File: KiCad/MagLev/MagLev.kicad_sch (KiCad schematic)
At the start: 71 parts, among them J1 FC681465S, Q11 MMBT3904, Q12 AOD442G, Q13 AOD442G, Q18 ZX5T1951GTA, Q5 ZX5T1951GTA, U10 DRV5505, U11 DRV5505, U12 DRV5505, U13 MCP1402, U14 MCP1402, U3 L78L05_SO8, U4 TL431A, U5 LM393, X1 L_Ferrite, X2 L_Ferrite, Y1 L_Ferrite, Y2 L_Ferrite, Y5 L_Ferrite, Y6 L_Ferrite, Y8 L_Ferrite, Y9 L_Ferrite

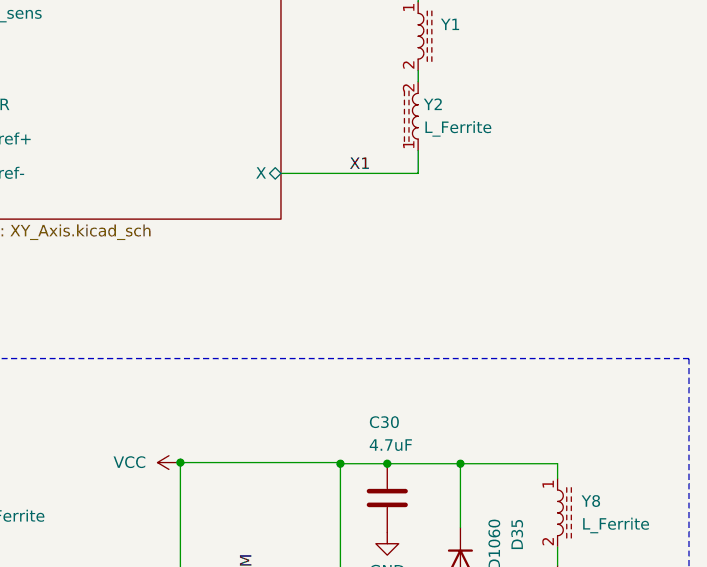
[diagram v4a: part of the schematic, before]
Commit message: Remove silkscreen components from back layer. Cleanup schematic and pcb.
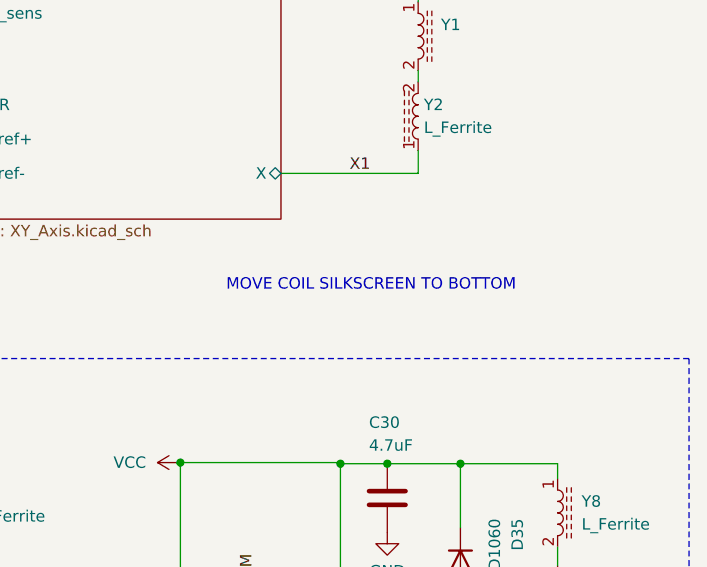
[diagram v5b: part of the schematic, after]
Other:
- note added: "MOVE COIL SILKSCREEN TO BOTTOM"
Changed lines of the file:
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@@
+    (effects (font (size 1.27 1.27)) (justify left bottom))
+  )
+  (text "MOVE COIL SILKSCREEN TO BOTTOM" (at 232.664 93.472 0)
     (effects (font (size 1.27 1.27)) (justify left bottom))
   )

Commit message: Update LED PCB reference after adding new LED schematic sheet.
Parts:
- DS1: PN (none) -> SML-LXT0805IW-TR; Part SML-LXT0805IW-TR -> (none)

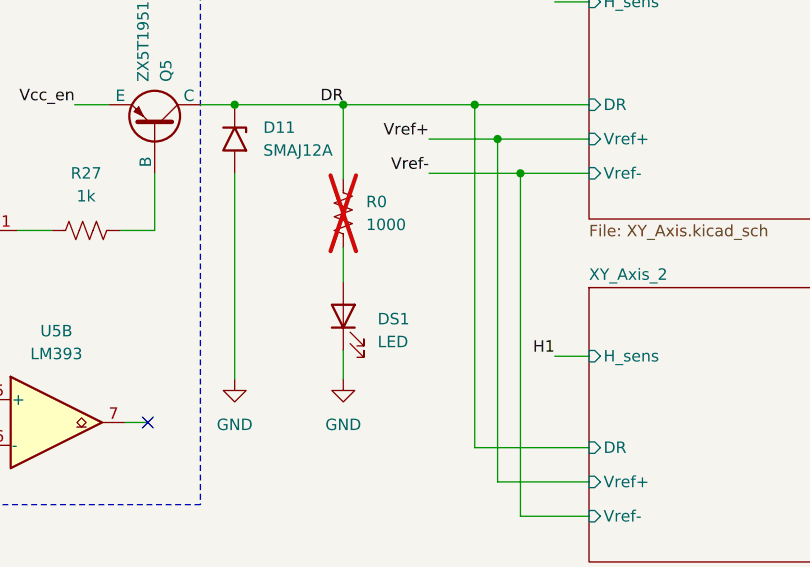
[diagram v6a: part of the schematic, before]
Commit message: Update BOM with JLCPCB PNs.
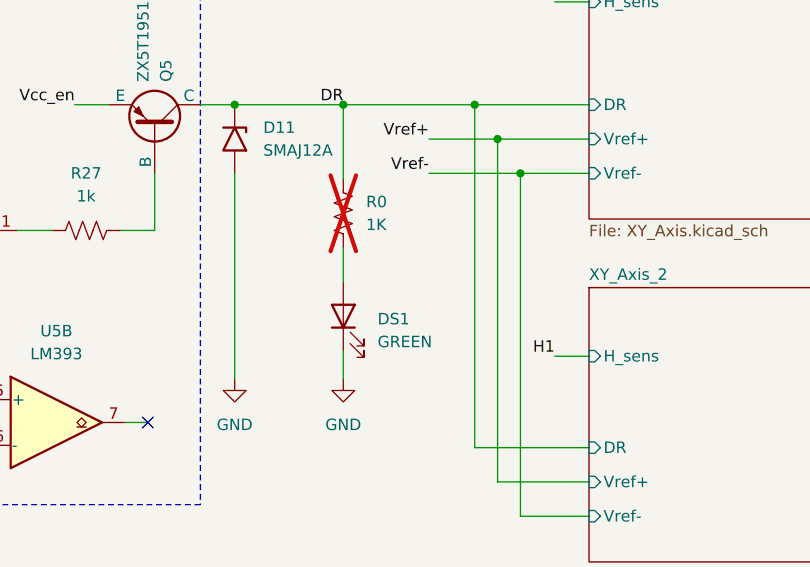
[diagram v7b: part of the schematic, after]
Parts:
- C10: JLC Part Number (none) -> C1710
- C19, C2, C20, C32, C33, C34, C35, C5: JLC Part Number (none) -> C28233
- C22, C23: JLC Part Number (none) -> C249974
- C29, C30, C31: JLC Part Number (none) -> C1779
- C9: JLC Part Number (none) -> C1740
- D34, D35: JLC Part Number (none) -> C174026
- DS1: value LED -> GREEN; JLC Part Number (none) -> C2297
- R0: value 1000 -> 1K
- R14, R16, R17, R7: JLC Part Number (none) -> C118848
- R15: JLC Part Number (none) -> C4328
- R18, R26: JLC Part Number (none) -> C25270
- R2, R27, R40, R51, R66: JLC Part Number (none) -> C17513
- R50: JLC Part Number (none) -> C17514
- R67: JLC Part Number (none) -> C17414
- U13, U14: JLC Part Number (none) -> C128573
- U3: JLC Part Number (none) -> C42738
- U4: JLC Part Number (none) -> C23892
- U5: JLC Part Number (none) -> C7955
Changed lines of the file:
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@@
       (effects (font (size 1.27 1.27)) hide)
     )
-    (property "JLC Part Number" "" (at 76.073 141.605 0)
+    (property "JLC Part Number" "C249974" (at 76.073 141.605 0)
       (effects (font (size 1.27 1.27)) hide)
     )
@@
       (effects (font (size 1.27 1.27)) hide)
     )
-    (property "JLC Part Number" "" (at 64.135 141.605 0)
+    (property "JLC Part Number" "C249974" (at 64.135 141.605 0)
       (effects (font (size 1.27 1.27)) hide)
     )
@@
       (effects (font (size 1.27 1.27)) hide)
     )
-    (property "JLC Part Number" "" (at 191.516 122.555 0)
+    (property "JLC Part Number" "C174026" (at 191.516 122.555 0)
       (effects (font (size 1.27 1.27)) hide)
     )
@@
       (effects (font (size 1.27 1.27)) hide)
     )
-    (property "JLC Part Number" "" (at 110.49 159.893 0)
+    (property "JLC Part Number" "C23892" (at 110.49 159.893 0)
       (effects (font (size 1.27 1.27)) hide)
     )
@@
       (effects (font (size 1.27 1.27)) hide)
     )
-    (property "JLC Part Number" "" (at 160.401 138.049 0)
+    (property "JLC Part Number" "C28233" (at 160.401 138.049 0)
       (effects (font (size 1.27 1.27)) hide)
     )
@@
       (effects (font (size 1.27 1.27)) hide)
     )
-    (property "JLC Part Number" "" (at 41.91 173.482 0)
+    (property "JLC Part Number" "C1740" (at 41.91 173.482 0)
       (effects (font (size 1.27 1.27)) hide)
     )
@@
       (effects (font (size 1.27 1.27)) hide)
     )
-    (property "JLC Part Number" "" (at 128.27 152.273 0)
+    (property "JLC Part Number" "C118848" (at 128.27 152.273 0)
       (effects (font (size 1.27 1.27)) hide)
     )
@@
       (effects (font (size 1.27 1.27)) hide)
     )
-    (property "JLC Part Number" "" (at 145.288 69.85 0)
+    (property "JLC Part Number" "C7955" (at 145.288 69.85 0)
       (effects (font (size 1.27 1.27)) hide)
     )
@@
       (effects (font (size 1.27 1.27)) hide)
     )
-    (property "JLC Part Number" "" (at 133.35 48.514 0)
+    (property "JLC Part Number" "C7955" (at 133.35 48.514 0)
       (effects (font (size 1.27 1.27)) hide)
     )
@@
       (effects (font (size 1.27 1.27)) hide)
     )
-    (property "JLC Part Number" "" (at 168.783 134.366 0)
+    (property "JLC Part Number" "C17513" (at 168.783 134.366 0)
       (effects (font (size 1.27 1.27)) hide)
     )
@@
       (effects (font (size 1.27 1.27)) hide)
     )
-    (property "JLC Part Number" "" (at 46.99 41.91 0)
+    (property "JLC Part Number" "C28233" (at 46.99 41.91 0)
       (effects (font (size 1.27 1.27)) hide)
     )
@@
       (effects (font (size 1.27 1.27)) hide)
     )
-    (property "JLC Part Number" "" (at 128.27 180.213 0)
+    (property "JLC Part Number" "C28233" (at 128.27 180.213 0)
       (effects (font (size 1.27 1.27)) hide)
     )
@@
       (effects (font (size 1.27 1.27)) hide)
     )
-    (property "JLC Part Number" "" (at 101.473 141.605 0)
+    (property "JLC Part Number" "C28233" (at 101.473 141.605 0)
       (effects (font (size 1.27 1.27)) hide)
     )
@@
       (effects (font (size 1.27 1.27)) hide)
     )
-    (property "JLC Part Number" "" (at 227.584 138.938 0)
+    (property "JLC Part Number" "C28233" (at 227.584 138.938 0)
       (effects (font (size 1.27 1.27)) hide)
     )
@@
       (effects (font (size 1.27 1.27)) hide)
     )
-    (property "JLC Part Number" "" (at 86.233 149.225 0)
+    (property "JLC Part Number" "C17514" (at 86.233 149.225 0)
       (effects (font (size 1.27 1.27)) hide)
     )
@@
       (effects (font (size 1.27 1.27)) hide)
     )
-    (property "JLC Part Number" "" (at 65.405 173.482 0)
+    (property "JLC Part Number" "C1710" (at 65.405 173.482 0)
       (effects (font (size 1.27 1.27)) hide)
     )
@@
       (effects (font (size 1.27 1.27)) (justify right))
     )
-    (property "Value" "LED" (at 180.975 60.8965 90)
+    (property "Value" "GREEN" (at 180.975 60.8965 90)
       (effects (font (size 1.27 1.27)) (justify right))
     )
@@
       (effects (font (size 1.27 1.27)) hide)
     )
-    (property "JLC Part Number" "" (at 177.165 58.039 0)
+    (property "JLC Part Number" "C2297" (at 177.165 58.039 0)
       (effects (font (size 1.27 1.27)) hide)
     )
@@
       (effects (font (size 1.27 1.27)) hide)
     )
-    (property "JLC Part Number" "" (at 235.966 135.255 0)
+    (property "JLC Part Number" "C17513" (at 235.966 135.255 0)
       (effects (font (size 1.27 1.27)) hide)
     )
@@
       (effects (font (size 1.27 1.27)) hide)
     )
-    (property "JLC Part Number" "" (at 56.388 80.518 0)
+    (property "JLC Part Number" "C17414" (at 56.388 80.518 0)
       (effects (font (size 1.27 1.27)) hide)
     )
@@
       (effects (font (size 1.27 1.27)) hide)
     )
-    (property "JLC Part Number" "" (at 63.5 85.09 0)
+    (property "JLC Part Number" "C17513" (at 63.5 85.09 0)
       (effects (font (size 1.27 1.27)) hide)
     )
@@
       (effects (font (size 1.27 1.27)) hide)
     )
-    (property "JLC Part Number" "" (at 116.84 45.974 0)
+    (property "JLC Part Number" "C118848" (at 116.84 45.974 0)
       (effects (font (size 1.27 1.27)) hide)
     )
@@
       (effects (font (size 1.27 1.27)) hide)
     )
-    (property "JLC Part Number" "" (at 76.2 41.656 0)
+    (property "JLC Part Number" "C28233" (at 76.2 41.656 0)
       (effects (font (size 1.27 1.27)) hide)
     )
@@
       (effects (font (size 1.27 1.27)) hide)
     )
-    (property "JLC Part Number" "" (at 183.769 115.443 0)
+    (property "JLC Part Number" "C1779" (at 183.769 115.443 0)
       (effects (font (size 1.27 1.27)) hide)
     )
@@
       (effects (font (size 1.27 1.27)) hide)
     )
-    (property "JLC Part Number" "" (at 125.73 63.754 0)
+    (property "JLC Part Number" "C118848" (at 125.73 63.754 0)
       (effects (font (size 1.27 1.27)) hide)
     )
@@
       (effects (font (size 1.27 1.27)) hide)
     )
-    (property "JLC Part Number" "" (at 29.718 87.122 0)
+    (property "JLC Part Number" "C7955" (at 29.718 87.122 0)
       (effects (font (size 1.27 1.27)) hide)
     )
@@
       (effects (font (size 1.27 1.27)) hide)
     )
-    (property "JLC Part Number" "" (at 78.613 96.52 0)
+    (property "JLC Part Number" "C17513" (at 78.613 96.52 0)
       (effects (font (size 1.27 1.27)) hide)
     )
@@
       (effects (font (size 1.27 1.27)) hide)
     )
-    (property "JLC Part Number" "" (at 114.3 135.763 0)
+    (property "JLC Part Number" "C25270" (at 114.3 135.763 0)
       (effects (font (size 1.27 1.27)) hide)
     )
@@
       (effects (font (size 1.27 1.27)) hide)
     )
-    (property "JLC Part Number" "" (at 178.181 138.176 0)
+    (property "JLC Part Number" "C128573" (at 178.181 138.176 0)
       (effects (font (size 1.27 1.27)) hide)
     )
@@
       (effects (font (size 1.27 1.27)) hide)
     )
-    (property "JLC Part Number" "" (at 88.773 141.605 0)
+    (property "JLC Part Number" "C1779" (at 88.773 141.605 0)
       (effects (font (size 1.27 1.27)) hide)
     )
@@
       (effects (font (size 1.27 1.27)) hide)
     )
-    (property "JLC Part Number" "" (at 148.59 48.514 0)
+    (property "JLC Part Number" "C17513" (at 148.59 48.514 0)
       (effects (font (size 1.27 1.27)) hide)
     )
@@
       (effects (font (size 1.27 1.27)) hide)
     )
-    (property "JLC Part Number" "" (at 113.03 56.134 0)
+    (property "JLC Part Number" "C4328" (at 113.03 56.134 0)
       (effects (font (size 1.27 1.27)) hide)
     )
@@
       (effects (font (size 1.27 1.27)) hide)
     )
-    (property "JLC Part Number" "" (at 53.975 163.957 0)
+    (property "JLC Part Number" "C42738" (at 53.975 163.957 0)
       (effects (font (size 1.27 1.27)) hide)
     )
@@
       (effects (font (size 1.27 1.27)) hide)
     )
-    (property "JLC Part Number" "" (at 128.27 135.763 0)
+    (property "JLC Part Number" "C28233" (at 128.27 135.763 0)
       (effects (font (size 1.27 1.27)) hide)
     )
@@
       (effects (font (size 1.27 1.27)) hide)
     )
-    (property "JLC Part Number" "" (at 245.364 139.065 0)
+    (property "JLC Part Number" "C128573" (at 245.364 139.065 0)
       (effects (font (size 1.27 1.27)) hide)
     )
@@
       (effects (font (size 1.27 1.27)) hide)
     )
-    (property "JLC Part Number" "" (at 128.27 167.513 0)
+    (property "JLC Part Number" "C118848" (at 128.27 167.513 0)
       (effects (font (size 1.27 1.27)) hide)
     )
@@
       (effects (font (size 1.27 1.27)) hide)
     )
-    (property "JLC Part Number" "" (at 19.05 42.418 0)
+    (property "JLC Part Number" "C28233" (at 19.05 42.418 0)
       (effects (font (size 1.27 1.27)) hide)
     )
@@
       (effects (font (size 1.27 1.27)) hide)
     )
-    (property "JLC Part Number" "" (at 250.571 116.332 0)
+    (property "JLC Part Number" "C1779" (at 250.571 116.332 0)
       (effects (font (size 1.27 1.27)) hide)
     )
@@
       (effects (font (size 1.27 1.27)) (justify left))
     )
-    (property "Value" "1000" (at 179.705 47.879 0)
+    (property "Value" "1K" (at 179.705 47.879 0)
       (effects (font (size 1.27 1.27)) (justify left))
     )
@@
       (effects (font (size 1.27 1.27)) hide)
     )
-    (property "JLC Part Number" "" (at 114.3 180.213 0)
+    (property "JLC Part Number" "C25270" (at 114.3 180.213 0)
       (effects (font (size 1.27 1.27)) hide)
     )
@@
       (effects (font (size 1.27 1.27)) hide)
     )
-    (property "JLC Part Number" "" (at 258.699 123.444 0)
-      (effects (font (size 1.27 1.27)) hide)
-    )
+    (property "JLC Part Number" "C174026" (at 258.699 123.444 0)
+      (effects (font (size 1.27 1.27)) hide)
+    )

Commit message: Add board art folder and upload svg files.
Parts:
- R14, R16, R17, R7: JLC Part Number C118848 -> C27834
- R50: JLC Part Number C17514 -> (none)
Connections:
- net at U5.6 (-): now also U5.7
- no-connect marks 3 -> 1
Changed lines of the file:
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@@
   (junction (at 152.019 97.79) (diameter 0) (color 0 0 0 0)
   )
-  (no_connect (at 135.128 72.39))
   (no_connect (at 135.128 67.31))
-  (no_connect (at 155.448 69.85))
   (wire (pts (xy 41.91 179.832) (xy 53.975 179.832))
     (stroke (width 0) (type default))
@@
     (stroke (width 0) (type default))
   )
+  (wire (pts (xy 137.668 72.136) (xy 137.668 72.39))
+    (stroke (width 0) (type default))
+  )
   (wire (pts (xy 27.178 94.742) (xy 27.178 101.092))
     (stroke (width 0) (type default))
@@
     (stroke (width 0) (type default))
   )
-  (wire (pts (xy 135.128 72.39) (xy 137.668 72.39))
-    (stroke (width 0) (type default))
-  )
   (wire (pts (xy 114.3 128.143) (xy 114.3 131.953))
     (stroke (width 0) (type default))
@@
     (stroke (width 0) (type default))
   )
+  (wire (pts (xy 155.448 76.708) (xy 134.366 76.708))
+    (stroke (width 0) (type default))
+  )
   (wire (pts (xy 46.99 38.1) (xy 46.99 30.988))
     (stroke (width 0) (type default))
@@
     (stroke (width 0) (type default))
   )
+  (wire (pts (xy 134.366 72.136) (xy 137.668 72.136))
+    (stroke (width 0) (type default))
+  )
   (wire (pts (xy 204.47 76.454) (xy 194.31 76.454))
     (stroke (width 0) (type default))
@@
     (stroke (width 0) (type default))
   )
+  (wire (pts (xy 134.366 76.708) (xy 134.366 72.136))
+    (stroke (width 0) (type default))
+  )
   (wire (pts (xy 258.699 112.522) (xy 250.571 112.522))
     (stroke (width 0) (type default))
@@
     (stroke (width 0) (type default))
   )
+  (wire (pts (xy 155.448 69.85) (xy 155.448 76.708))
+    (stroke (width 0) (type default))
+  )
   (wire (pts (xy 63.5 88.9) (xy 63.5 89.916))
     (stroke (width 0) (type default))
@@
       (effects (font (size 1.27 1.27)) hide)
     )
-    (property "JLC Part Number" "C118848" (at 128.27 152.273 0)
+    (property "JLC Part Number" "C27834" (at 128.27 152.273 0)
       (effects (font (size 1.27 1.27)) hide)
     )
@@
       (effects (font (size 1.27 1.27)) hide)
     )
-    (property "JLC Part Number" "C17514" (at 86.233 149.225 0)
+    (property "JLC Part Number" "" (at 86.233 149.225 0)
       (effects (font (size 1.27 1.27)) hide)
     )
@@
       (effects (font (size 1.27 1.27)) hide)
     )
-    (property "JLC Part Number" "C118848" (at 116.84 45.974 0)
+    (property "JLC Part Number" "C27834" (at 116.84 45.974 0)
       (effects (font (size 1.27 1.27)) hide)
     )
@@
       (effects (font (size 1.27 1.27)) hide)
     )
-    (property "JLC Part Number" "C118848" (at 125.73 63.754 0)
+    (property "JLC Part Number" "C27834" (at 125.73 63.754 0)
       (effects (font (size 1.27 1.27)) hide)
     )
@@
       (effects (font (size 1.27 1.27)) hide)
     )
-    (property "JLC Part Number" "C118848" (at 128.27 167.513 0)
+    (property "JLC Part Number" "C27834" (at 128.27 167.513 0)
       (effects (font (size 1.27 1.27)) hide)
     )
